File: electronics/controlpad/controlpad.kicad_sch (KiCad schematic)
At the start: 24 parts, among them J1 USB - Host, SW1 START, SW10 0, SW11 8, SW12 10, SW13 11, SW14 12, SW15 13, SW16 14, SW17 15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

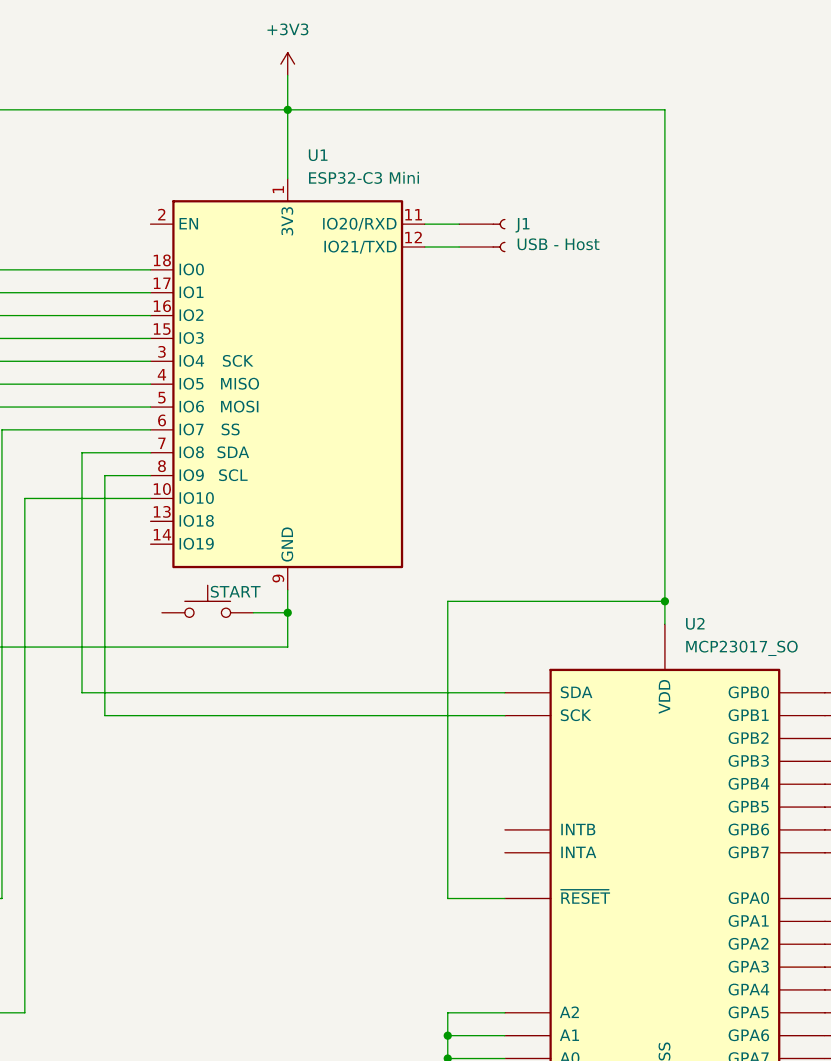
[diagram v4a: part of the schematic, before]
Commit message: Removing start button from GPIO10, now using I2C
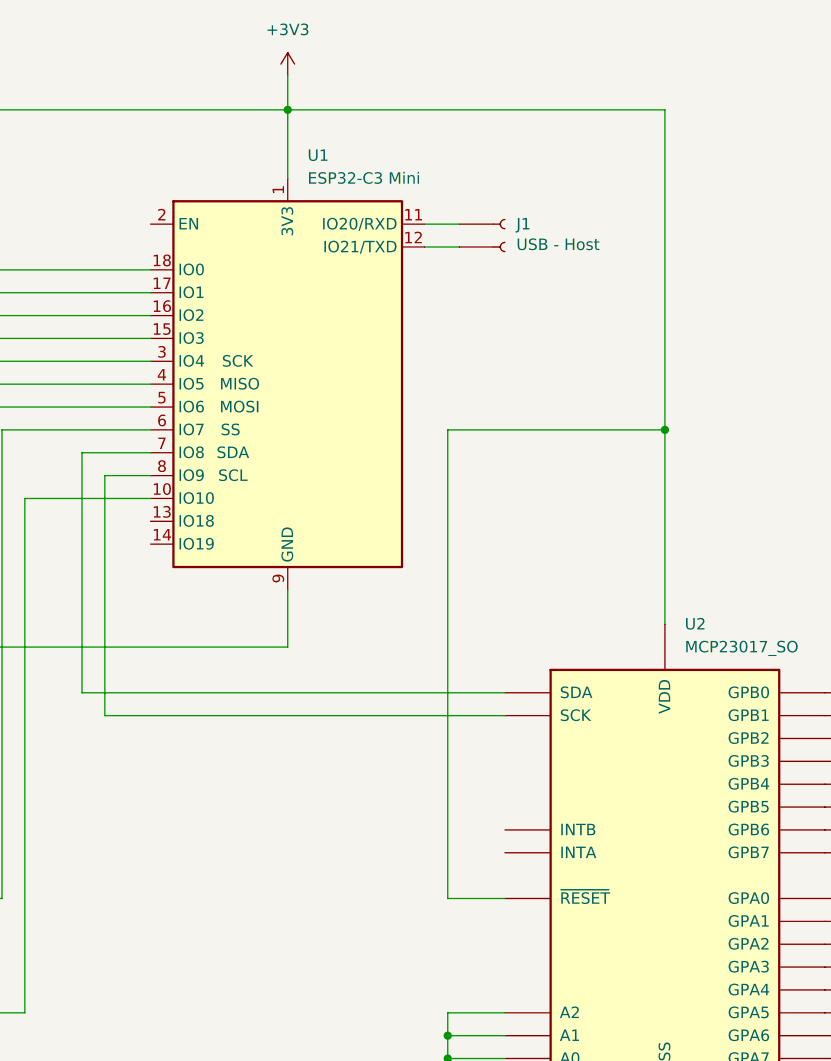
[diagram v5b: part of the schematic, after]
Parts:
- removed SW1: START, symbol Switch:SW_Push
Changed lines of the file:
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@@
 	)
 	(junction
-		(at 163.83 91.44)
-		(diameter 0)
-		(color 0 0 0 0)
-	)
-	(junction
 		(at 195.58 142.24)
 		(diameter 0)
@@
 	)
 	(junction
-		(at 121.92 92.71)
-		(diameter 0)
-		(color 0 0 0 0)
-	)
-	(junction
 		(at 50.8 50.8)
 		(diameter 0)
@@
 	)
 	(junction
+		(at 163.83 72.39)
+		(diameter 0)
+		(color 0 0 0 0)
+	)
+	(junction
 		(at 64.77 71.12)
 		(diameter 0)
@@
 	(wire
 		(pts
-			(xy 163.83 91.44) (xy 163.83 93.98)
-		)
-		(stroke
-			(width 0)
-			(type default)
-			(color 255 0 0 1)
-		)
-	)
-	(wire
-		(pts
 			(xy 195.58 137.16) (xy 195.58 139.7)
 		)
@@
 	(wire
 		(pts
-			(xy 121.92 90.17) (xy 121.92 92.71)
+			(xy 121.92 90.17) (xy 121.92 96.52)
 		)
 		(stroke
@@
 	(wire
 		(pts
-			(xy 118.11 92.71) (xy 121.92 92.71)
-		)
-		(stroke
-			(width 0)
-			(type default)
-			(color 0 0 0 1)
-		)
-	)
-	(wire
-		(pts
-			(xy 121.92 92.71) (xy 121.92 96.52)
-		)
-		(stroke
-			(width 0)
-			(type default)
-			(color 0 0 0 1)
-		)
-	)
-	(wire
-		(pts
 			(xy 191.77 132.08) (xy 195.58 132.08)
 		)
@@
 	(wire
 		(pts
-			(xy 139.7 91.44) (xy 139.7 124.46)
+			(xy 139.7 72.39) (xy 139.7 124.46)
 		)
 		(stroke
@@
 	(wire
 		(pts
-			(xy 139.7 91.44) (xy 163.83 91.44)
+			(xy 139.7 72.39) (xy 163.83 72.39)
 		)
 		(stroke
@@
 	(wire
 		(pts
-			(xy 163.83 36.83) (xy 163.83 91.44)
+			(xy 163.83 36.83) (xy 163.83 72.39)
 		)
 		(stroke
@@
 	(wire
 		(pts
+			(xy 163.83 72.39) (xy 163.83 93.98)
+		)
+		(stroke
+			(width 0)
+			(type default)
+			(color 255 0 0 1)
+		)
+	)
+	(wire
+		(pts
 			(xy 99.06 74.93) (xy 99.06 101.6)
 		)
@@
 					(unit 1)
 				)
-			)
-		)
-	)
-	(symbol
-		(lib_id "Switch:SW_Push")
-		(at 113.03 92.71 0)
-		(unit 1)
-		(exclude_from_sim no)
-		(in_bom yes)
-		(on_board yes)
-		(dnp no)
-		(property "Reference" "SW1"
-			(at 113.03 85.09 0)
-			(effects
-				(font
-					(size 1.27 1.27)
-				)
-				(hide yes)
-			)
-		)
-		(property "Value" "START"
-			(at 116.078 90.424 0)
-			(effects
-				(font
-					(size 1.27 1.27)
-				)
-			)
-		)
-		(property "Footprint" ""
-			(at 113.03 87.63 0)
-			(effects
-				(font
-					(size 1.27 1.27)
-				)
-				(hide yes)
-			)
-		)
-		(property "Datasheet" "~"
-			(at 113.03 87.63 0)
-			(effects
-				(font
-					(size 1.27 1.27)
-				)
-				(hide yes)
-			)
-		)
-		(property "Description" "Push button switch, generic, two pins"
-			(at 113.03 92.71 0)
-			(effects
-				(font
-					(size 1.27 1.27)
-				)
-				(hide yes)
-			)
-		)
-		(pin "1"
-		)
-		(pin "2"
-		)
-		(instances
-			(project ""
-				(path "/c06f4dac-aef6-4417-a281-a2a0987c6210"
-					(reference "SW1")
-					(unit 1)
-				)
